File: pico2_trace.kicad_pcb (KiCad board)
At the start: 2 copper layers, 92 x 64 mm, 56 parts, among them J10 SWD, J1B BREAKOUT, J2B BREAKOUT, J3 MIPI-20, J5 USB-A HOST, J6 CORTEX-10, J7 JST-SH-3 DEBUG_PROBE, J8 USB-MICROB PWR, J9 USB-MICROB DEV, SW1 RESET

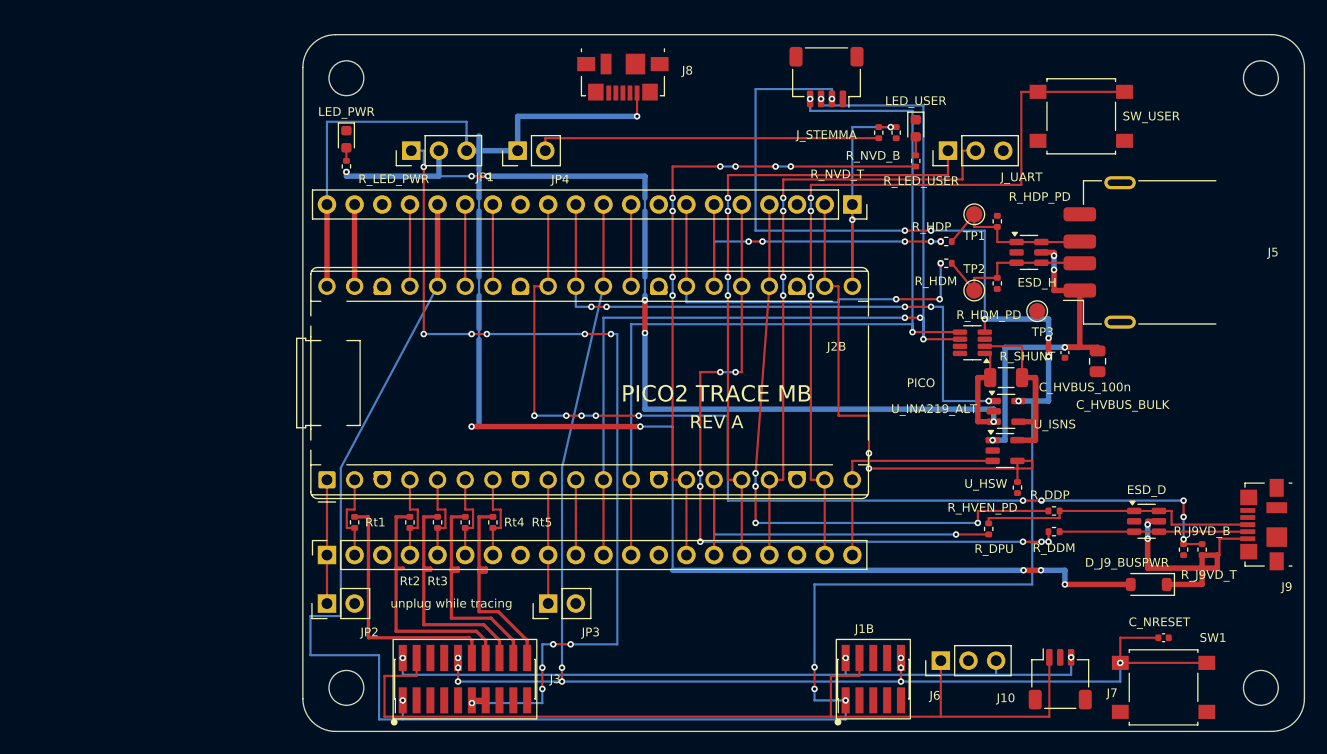
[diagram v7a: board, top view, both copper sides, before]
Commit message: pcb: widen VBUS_NET, add GND pours + stitching vias
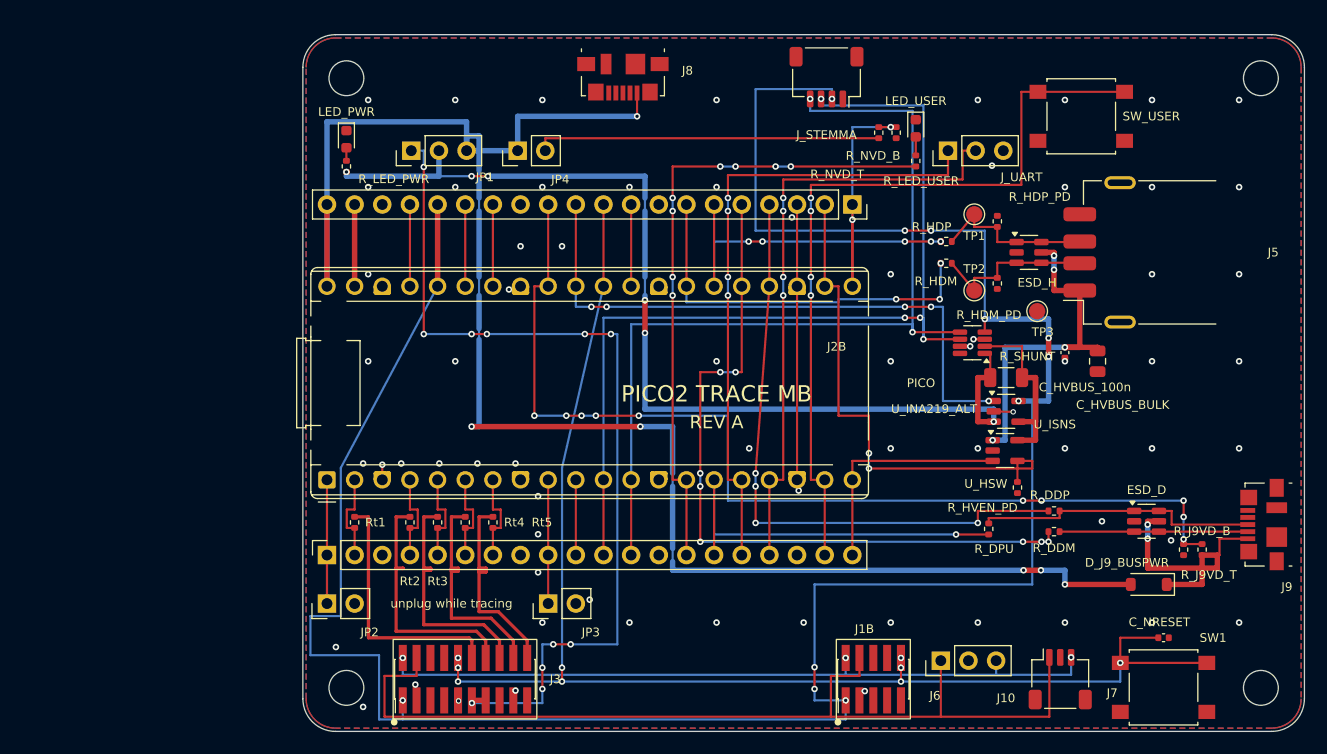
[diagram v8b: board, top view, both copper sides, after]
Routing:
- net GND: track 0.00 -> 30.5 mm, vias 0 -> 69
- added copper zone on B.Cu, net GND
- added copper zone on F.Cu, net GND
